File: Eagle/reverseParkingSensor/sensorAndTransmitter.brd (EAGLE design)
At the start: 46 x 50.8 mm, 29 parts, among them IC1 LM393N, IC3 MEGA8-P, Q1 BC558B, T1 BPX81, X1 YH-55-10

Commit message: final pcb for sensor and transmitter
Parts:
- added LED1: (no value), led:LED3MM
- added R6: 220, resistor:0207/10
- moved C14 16.6 mm to (64.1, 75.6)
- moved X1 13.9 mm to (51.4, 27.3)
- moved R3 8.47 mm to (40.6, 32.4)
- moved JP2 7.85 mm to (41.9, 29.8)
- moved T1 7.85 mm to (37.5, 29.8)
- moved R5 7.24 mm to (31.8, 32.4)
- moved IC10 6.75 mm to (60.3, 57.1), turned to 90 degrees
- moved R11 3.81 mm to (60.3, 53.3)
- moved C16 2.84 mm to (34.3, 72.4), turned to 0 degrees
- moved IC4 2.54 mm to (35.6, 71.1), turned to 180 degrees
- moved C15 2.29 mm to (36.8, 70.5), turned to 180 degrees
- moved U$2 0.64 mm to (57.8, 69.8)
- moved R4 0.63 mm to (38.7, 40.6)
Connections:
- new net N$6: IC3.15, R6.1
- new net N$7: LED1.A, R6.2
- net GND: now also LED1.K
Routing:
- net GND: track 182.3 -> 210.8 mm, vias 2 -> 4
- net +5V: track 128.1 -> 144.7 mm
- net PB3: track 11.0 -> 19.2 mm
- net +12V: track 76.9 -> 69.2 mm
- net PB4: track 14.5 -> 22.1 mm
- net PB5: track 18.0 -> 25.4 mm
- net N$4: track 2.80 -> 9.57 mm
- net +3V3: track 30.7 -> 24.3 mm
- net N$5: track 9.30 -> 15.5 mm
- net N$3: track 32.4 -> 35.6 mm
- net N$6: track 0.00 -> 1.55 mm
- net N$7: track 0.00 -> 1.35 mm
- net NRF_CSN: track 24.4 -> 23.6 mm
- net NRF_SCK: track 3.81 -> 3.17 mm
- net NRF_MOSI: track 17.6 -> 16.9 mm
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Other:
- board size 46 x 50.8 mm -> 42.2 x 52.1 mm
- board text added: "+"
- board text added: "Reverse Parking 1.1"
- board text removed: "SAJDAK.IT"

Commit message: final pcb
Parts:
- added JP1: (no value), jumper:JP1
- R4: device resistor:0204V -> resistor:0204/5
- R6: device resistor:0207/10 -> resistor:0204V
- moved LED1 21.6 mm to (41.9, 39.4), turned to 180 degrees
- moved R6 20.3 mm to (39.4, 41.9), turned to 180 degrees
- moved R11 10.6 mm to (63.5, 43.2), turned to 90 degrees
- moved U$2 5.43 mm to (59.7, 64.8), turned to 180 degrees
- moved R4 4.96 mm to (35.6, 36.8), turned to 180 degrees
- moved IC10 4.84 mm to (62.2, 52.7), turned to 180 degrees
- moved C6 2.62 mm to (58.4, 50.8), turned to 0 degrees
- moved C14 2.29 mm to (62.9, 73.7), turned to 270 degrees
- moved X1 1.27 mm to (51.4, 28.6)
- moved JP2 0.63 mm to (41.9, 29.2)
- moved R5 0.63 mm to (31.8, 31.8)
- moved T1 0.63 mm to (37.5, 29.2)
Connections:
- new net N$8: IC3.15, X1.4
- new net N$9: IC3.16, X1.2
- net +5V: now also JP1.2; no longer X1.5
- net GND: now also JP1.1, R6.2; no longer LED1.K, X1.3
- net N$5: now also IC3.14; no longer IC3.16
- net N$6: now also LED1.K; no longer IC3.15
- net N$7: now also IC3.13; no longer R6.2
- net PB3: now also X1.6; no longer X1.2
- net PB4: now also X1.5; no longer X1.4
- net PB5: now also X1.3; no longer X1.6
- net UPHOLD: now also IC3.12; no longer IC3.14
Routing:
- net N$11: track 0.00 -> 28.8 mm
- net +3V3: track 24.3 -> 8.56 mm
- net NRF_CSN: track 23.6 -> 10.8 mm
- net N$9: track 0.00 -> 11.2 mm
- net NRF_MOSI: track 16.9 -> 6.88 mm
- net PB5: track 25.4 -> 34.8 mm
- net NRF_CE: track 3.17 -> 11.2 mm
- net +5V: track 144.7 -> 136.7 mm
- net N$5: track 15.5 -> 8.20 mm
- net N$4: track 9.57 -> 3.07 mm
- net GND: track 210.8 -> 204.7 mm
- net NRF_IRQ: track 8.26 -> 2.54 mm
- net N$8: track 0.00 -> 5.27 mm
- net N$17: track 7.77 -> 12.8 mm
- net PB3: track 19.2 -> 14.6 mm
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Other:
- board size 42.2 x 52.1 mm -> 42.9 x 54 mm
- board text added: "in"
- board text removed: "C1"
- board text removed: "C2"
- board text removed: "C3"
- board text removed: "C4"
- board text removed: "C5"
- board text removed: "C6"
- board text removed: "C7"
- board text removed: "C8"
- board text removed: "IC1"
- board text removed: "IC2"
- board text removed: "IC3"
- board text removed: "IC4"
- board text removed: "IC5"
- board text removed: "IC6"
- board text removed: "J1"
- board text removed: "J2"
- board text removed: "J3"
- board text removed: "J4"
- board text removed: "JP11"
- board text removed: "JP12"
- board text removed: "JP13"
- board text removed: "JP3"
- board text removed: "JP4"
- board text removed: "JP6"
- board text removed: "Q1"
- board text removed: "R1"
- board text removed: "R10"
- board text removed: "R11"
- board text removed: "R12"
- board text removed: "R13"
- board text removed: "R14"
- board text removed: "R15"
- board text removed: "R16"
- board text removed: "R17"
- board text removed: "R18"
- board text removed: "R19"
- board text removed: "R2"
- board text removed: "R3"
- board text removed: "R4"
- board text removed: "R5"
- board text removed: "R6"
- board text removed: "R7"
- board text removed: "R8"
- board text removed: "R9"
- board text removed: "U$1"
- board text removed: "U$3"
- board text removed: "X3"

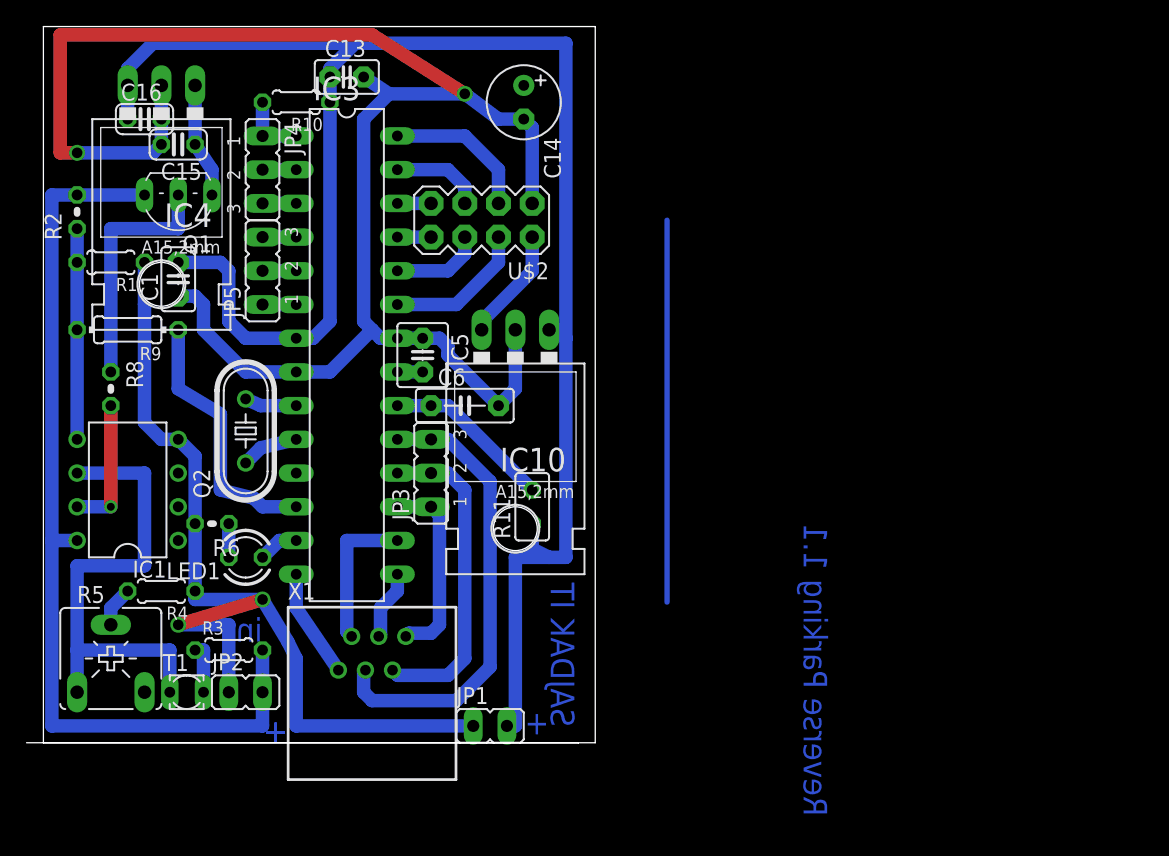
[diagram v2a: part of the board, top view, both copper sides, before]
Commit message: sime test only sending increasing integers and displays is
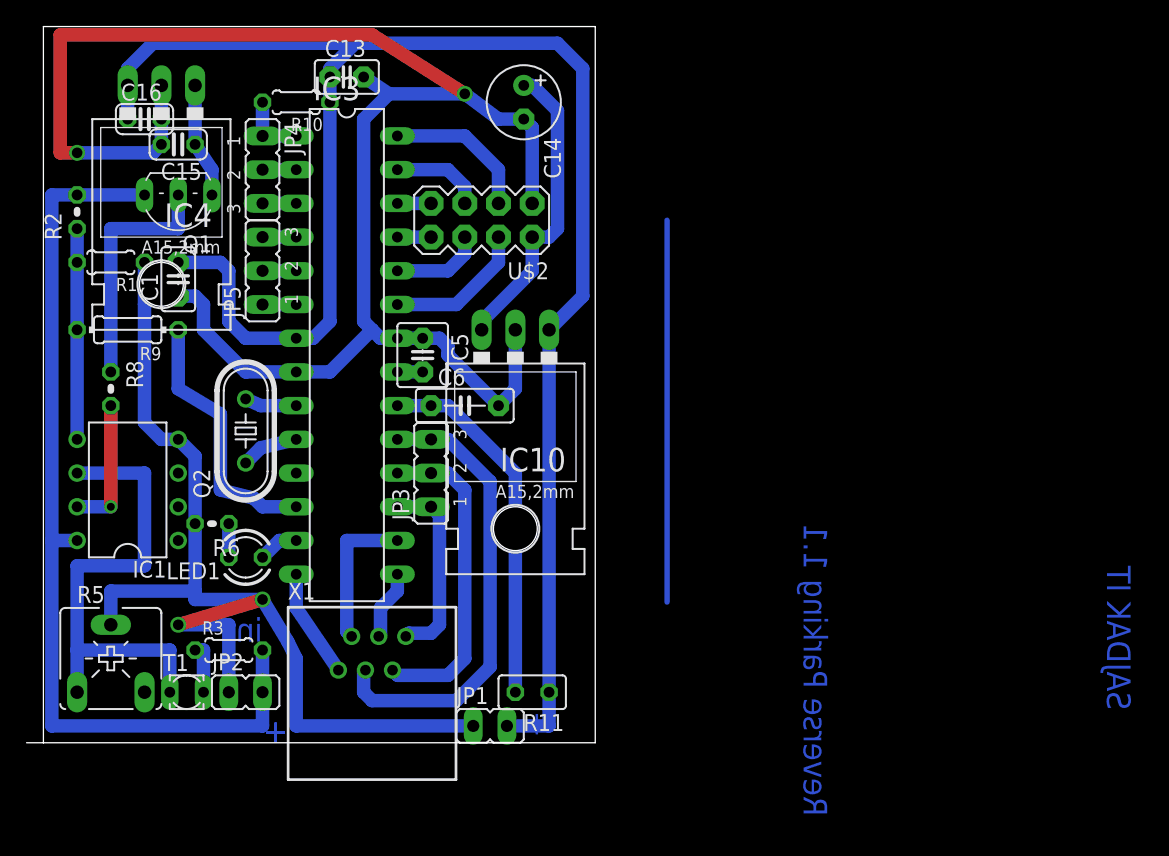
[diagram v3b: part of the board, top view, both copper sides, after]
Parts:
- removed R4: 22k, resistor:0204/5
- R2: value 47k -> 220k
- R5: value (none) -> 0-200k
- moved R11 14.0 mm to (63.5, 29.2), turned to 180 degrees
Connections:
- removed net N$4: R4.2, R5.S
- net GND: now also R5.S; no longer R4.1
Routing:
- net N$17: track 12.8 -> 27.5 mm
- net +3V3: track 8.56 -> 23.0 mm
- net GND: track 204.7 -> 213.6 mm
- net +5V: track 136.7 -> 132.4 mm
- net N$4: track 3.07 -> 0.00 mm
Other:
- outline, holes or cut-outs redrawn
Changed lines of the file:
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@@
 <board>
 <plain>
-<wire x1="26.67" y1="25.4" x2="66.98" y2="25.4" width="0" layer="20"/>
-<wire x1="66.98" y1="25.4" x2="68.25" y2="25.4" width="0" layer="20"/>
+<wire x1="26.67" y1="25.4" x2="68.25" y2="25.4" width="0" layer="20"/>
 <wire x1="68.25" y1="25.4" x2="68.25" y2="79.365" width="0" layer="20"/>
 <wire x1="68.25" y1="79.365" x2="26.67" y2="79.365" width="0" layer="20"/>
@@
 <rectangle x1="28.8163" y1="77.8383" x2="29.0449" y2="77.9145" layer="200"/>
 <rectangle x1="28.8925" y1="77.9145" x2="29.0449" y2="77.9907" layer="200"/>
-<text x="66.675" y="37.465" size="1.778" layer="16" rot="MR270">SAJDAK IT</text>
+<text x="108.585" y="38.735" size="1.778" layer="16" rot="MR270">SAJDAK IT</text>
 <dimension x1="70.79" y1="78.73" x2="70.79" y2="26.67" x3="80.01" y3="52.7" textsize="1.778" layer="16"/>
 <dimension x1="25.4" y1="27.94" x2="68.25" y2="27.94" x3="46.825" y3="16.51" textsize="1.778" layer="16"/>
 <text x="45.085" y="25.4" size="1.778" layer="16" rot="MR0">+</text>
 <text x="85.725" y="41.91" size="1.778" layer="16" rot="MR270">Reverse Parking 1.1</text>
-<wire x1="25.4" y1="25.4" x2="66.98" y2="25.4" width="0" layer="20"/>
+<wire x1="25.4" y1="25.4" x2="26.67" y2="25.4" width="0" layer="20"/>
 <text x="45.085" y="25.4" size="1.778" layer="16" rot="MR0">+</text>
 <text x="64.77" y="26.035" size="1.778" layer="16" rot="MR0">+</text>
@@
 <element name="IC1" library="linear" package="DIL08" value="LM393N" x="33.02" y="44.45" rot="R90"/>
 <element name="R1" library="resistor" package="0204/5" value="47k" x="31.75" y="61.595" rot="R180"/>
-<element name="R2" library="resistor" package="0204V" value="47k" x="29.21" y="65.405" rot="R90"/>
+<element name="R2" library="resistor" package="0204V" value="220k" x="29.21" y="65.405" rot="R90"/>
 <element name="T1" library="opto-trans-siemens" package="BPX81" value="BPX81" x="37.465" y="29.21">
 <attribute name="MF" value="" x="37.465" y="29.21" size="1.778" layer="27" display="off"/>
@@
 </element>
 <element name="R3" library="resistor" package="0204/5" value="10k" x="40.64" y="32.385"/>
-<element name="R4" library="resistor" package="0204/5" value="22k" x="35.56" y="36.83" rot="R180"/>
-<element name="R5" library="pot" package="CA6V" value="" x="31.75" y="31.75"/>
+<element name="R5" library="pot" package="CA6V" value="0-200k" x="31.75" y="31.75"/>
 <element name="IC10" library="v-reg" package="78XXL" value="" x="62.23" y="52.705" rot="R180"/>
 <element name="C13" library="capacitor-wima" package="C2.5-2" value="0.1uF" x="49.53" y="75.565"/>
@@
 <element name="C1" library="capacitor-wima" package="C2.5-2" value="100nF" x="36.83" y="60.325" rot="R90"/>
 <element name="C5" library="capacitor-wima" package="C2.5-4" value="100nF" x="55.245" y="54.61" rot="R270"/>
-<element name="R11" library="resistor" package="V526-0" value="10uH" x="63.5" y="43.18" rot="R90"/>
+<element name="R11" library="resistor" package="V526-0" value="10uH" x="63.5" y="29.21" rot="R180"/>
 <element name="C6" library="capacitor-wima" package="C5B2.5" value="100nF" x="58.42" y="50.8"/>
 <element name="JP3" library="jumper" package="JP2" value="" x="55.88" y="45.72" rot="R90"/>
@@
 <wire x1="40.64" y1="57.15" x2="41.91" y2="55.88" width="1.016" layer="16"/>
 <wire x1="41.91" y1="55.88" x2="45.72" y2="55.88" width="1.016" layer="16"/>
-<wire x1="64.77" y1="39.37" x2="62.23" y2="39.37" width="1.016" layer="16"/>
-<wire x1="64.77" y1="39.37" x2="66.04" y2="39.37" width="1.016" layer="16"/>
-<wire x1="66.04" y1="55.88" x2="66.04" y2="39.37" width="1.016" layer="16"/>
-<wire x1="66.04" y1="55.88" x2="66.04" y2="78.105" width="1.016" layer="16"/>
-<wire x1="50.165" y1="78.105" x2="66.04" y2="78.105" width="1.016" layer="16"/>
 <wire x1="50.165" y1="78.105" x2="48.26" y2="76.2" width="1.016" layer="16"/>
 <wire x1="48.26" y1="76.2" x2="48.26" y2="75.565" width="1.016" layer="16"/>
 <wire x1="33.02" y1="72.39" x2="33.02" y2="74.93" width="1.016" layer="16"/>
 <wire x1="33.02" y1="74.93" x2="33.02" y2="76.2" width="1.016" layer="16"/>
-<wire x1="34.925" y1="78.105" x2="50.165" y2="78.105" width="1.016" layer="16"/>
+<wire x1="49.53" y1="78.105" x2="34.925" y2="78.105" width="1.016" layer="16"/>
+<wire x1="49.53" y1="78.105" x2="50.165" y2="78.105" width="1.016" layer="16"/>
 <wire x1="33.02" y1="76.2" x2="34.925" y2="78.105" width="1.016" layer="16"/>
 <contactref element="JP1" pad="2"/>
-<wire x1="62.23" y1="39.37" x2="62.23" y2="26.67" width="1.016" layer="16"/>
-<wire x1="62.23" y1="26.67" x2="61.595" y2="26.67" width="1.016" layer="16"/>
-<wire x1="64.77" y1="56.515" x2="65.405" y2="56.515" width="1.016" layer="16"/>
-<wire x1="65.405" y1="56.515" x2="66.04" y2="55.88" width="1.016" layer="16"/>
-<wire x1="63.5" y1="41.91" x2="63.5" y2="40.005" width="1.016" layer="16"/>
-<wire x1="63.5" y1="40.005" x2="64.77" y2="39.37" width="1.016" layer="16"/>
+<wire x1="64.77" y1="26.67" x2="64.77" y2="29.21" width="1.016" layer="16"/>
+<wire x1="64.77" y1="26.67" x2="61.595" y2="26.67" width="1.016" layer="16"/>
+<wire x1="64.77" y1="29.21" x2="64.77" y2="56.515" width="1.016" layer="16"/>
+<wire x1="64.77" y1="56.515" x2="67.31" y2="59.055" width="1.016" layer="16"/>
+<wire x1="67.31" y1="59.055" x2="67.31" y2="76.2" width="1.016" layer="16"/>
+<wire x1="67.31" y1="76.2" x2="65.405" y2="78.105" width="1.016" layer="16"/>
+<wire x1="65.405" y1="78.105" x2="49.53" y2="78.105" width="1.016" layer="16"/>
 </signal>
 <signal name="N$1">
@@
 <contactref element="C16" pad="2"/>
 <contactref element="IC1" pad="4"/>
-<contactref element="R4" pad="1"/>
 <contactref element="R1" pad="1"/>
 <contactref element="JP2" pad="1"/>
@@
 <wire x1="40.64" y1="29.21" x2="40.64" y2="34.29" width="1.016" layer="16"/>
 <contactref element="R6" pad="2"/>
-<wire x1="38.1" y1="46.99" x2="38.1" y2="41.91" width="1.016" layer="16"/>
-<wire x1="38.1" y1="36.83" x2="38.1" y2="41.91" width="1.016" layer="16"/>
+<wire x1="38.1" y1="41.91" x2="38.1" y2="46.99" width="1.016" layer="16"/>
 <wire x1="40.64" y1="34.29" x2="36.83" y2="34.29" width="1.016" layer="16"/>
 <via x="36.83" y="34.29" extent="1-16" drill="0.8" shape="square"/>
 <wire x1="36.83" y1="34.29" x2="43.18" y2="36.195" width="1.016" layer="1"/>
 <via x="43.18" y="36.195" extent="1-16" drill="0.8" shape="square"/>
-<wire x1="38.1" y1="36.195" x2="43.18" y2="36.195" width="1.016" layer="16"/>
-<wire x1="38.1" y1="36.195" x2="38.1" y2="36.83" width="1.016" layer="16"/>
+<wire x1="43.18" y1="36.195" x2="38.1" y2="36.195" width="1.016" layer="16"/>
 <wire x1="43.18" y1="36.195" x2="45.085" y2="33.02" width="1.016" layer="16"/>
 <wire x1="45.085" y1="33.02" x2="45.72" y2="31.75" width="1.016" layer="16"/>
@@
 <wire x1="57.15" y1="55.245" x2="57.15" y2="54.61" width="1.016" layer="16"/>
 <wire x1="57.15" y1="54.61" x2="60.96" y2="50.8" width="1.016" layer="16"/>
+<contactref element="R5" pad="S"/>
+<wire x1="38.1" y1="36.83" x2="38.1" y2="36.195" width="1.016" layer="16"/>
+<wire x1="38.1" y1="36.83" x2="38.1" y2="41.91" width="1.016" layer="16"/>
+<wire x1="31.75" y1="34.29" x2="31.75" y2="36.83" width="1.016" layer="16"/>
+<wire x1="31.75" y1="36.83" x2="38.1" y2="36.83" width="1.016" layer="16"/>
 </signal>
 <signal name="N$2">
@@
 <wire x1="36.195" y1="32.385" x2="29.21" y2="32.385" width="1.016" layer="16"/>
 </signal>
-<signal name="N$4">
-<contactref element="R4" pad="2"/>
-<contactref element="R5" pad="S"/>
-<wire x1="33.02" y1="36.83" x2="31.75" y2="35.56" width="1.016" layer="16"/>
-<wire x1="31.75" y1="35.56" x2="31.75" y2="34.29" width="1.016" layer="16"/>
-</signal>
 <signal name="+3V3">
 <contactref element="IC10" pad="OUT"/>
@@
 <wire x1="59.69" y1="56.515" x2="59.69" y2="57.15" width="1.016" layer="16"/>
 <wire x1="59.69" y1="57.15" x2="63.5" y2="60.96" width="1.016" layer="16"/>
-<wire x1="63.5" y1="60.96" x2="63.5" y2="63.5" width="1.016" layer="16"/>
-<wire x1="63.5" y1="63.5" x2="62.865" y2="74.93" width="0" layer="19" extent="1-1"/>
+<wire x1="63.5" y1="63.5" x2="63.5" y2="60.96" width="1.016" layer="16"/>
+<wire x1="62.865" y1="74.93" x2="63.5" y2="74.93" width="1.016" layer="16"/>
+<wire x1="65.405" y1="73.025" x2="65.405" y2="64.135" width="1.016" layer="16"/>
+<wire x1="65.405" y1="64.135" x2="64.77" y2="63.5" width="1.016" layer="16"/>
+<wire x1="64.77" y1="63.5" x2="63.5" y2="63.5" width="1.016" layer="16"/>
+<wire x1="63.5" y1="74.93" x2="65.405" y2="73.025" width="1.016" layer="16"/>
 </signal>
 <signal name="NRF_CE">
@@
 <contactref element="C6" pad="1"/>
 <wire x1="53.34" y1="50.8" x2="55.88" y2="50.8" width="1.016" layer="16"/>
-<wire x1="55.88" y1="50.8" x2="57.15" y2="50.8" width="1.016" layer="16"/>
-<wire x1="57.15" y1="50.8" x2="63.5" y2="44.45" width="1.016" layer="16"/>
+<wire x1="57.15" y1="50.8" x2="55.88" y2="50.8" width="1.016" layer="16"/>
+<wire x1="62.23" y1="29.21" x2="62.23" y2="45.72" width="1.016" layer="16"/>
+<wire x1="62.23" y1="45.72" x2="57.15" y2="50.8" width="1.016" layer="16"/>
 </signal>
 <signal name="N$59">
